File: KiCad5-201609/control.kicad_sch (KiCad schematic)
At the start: 23 parts, among them U304 DRV777DR

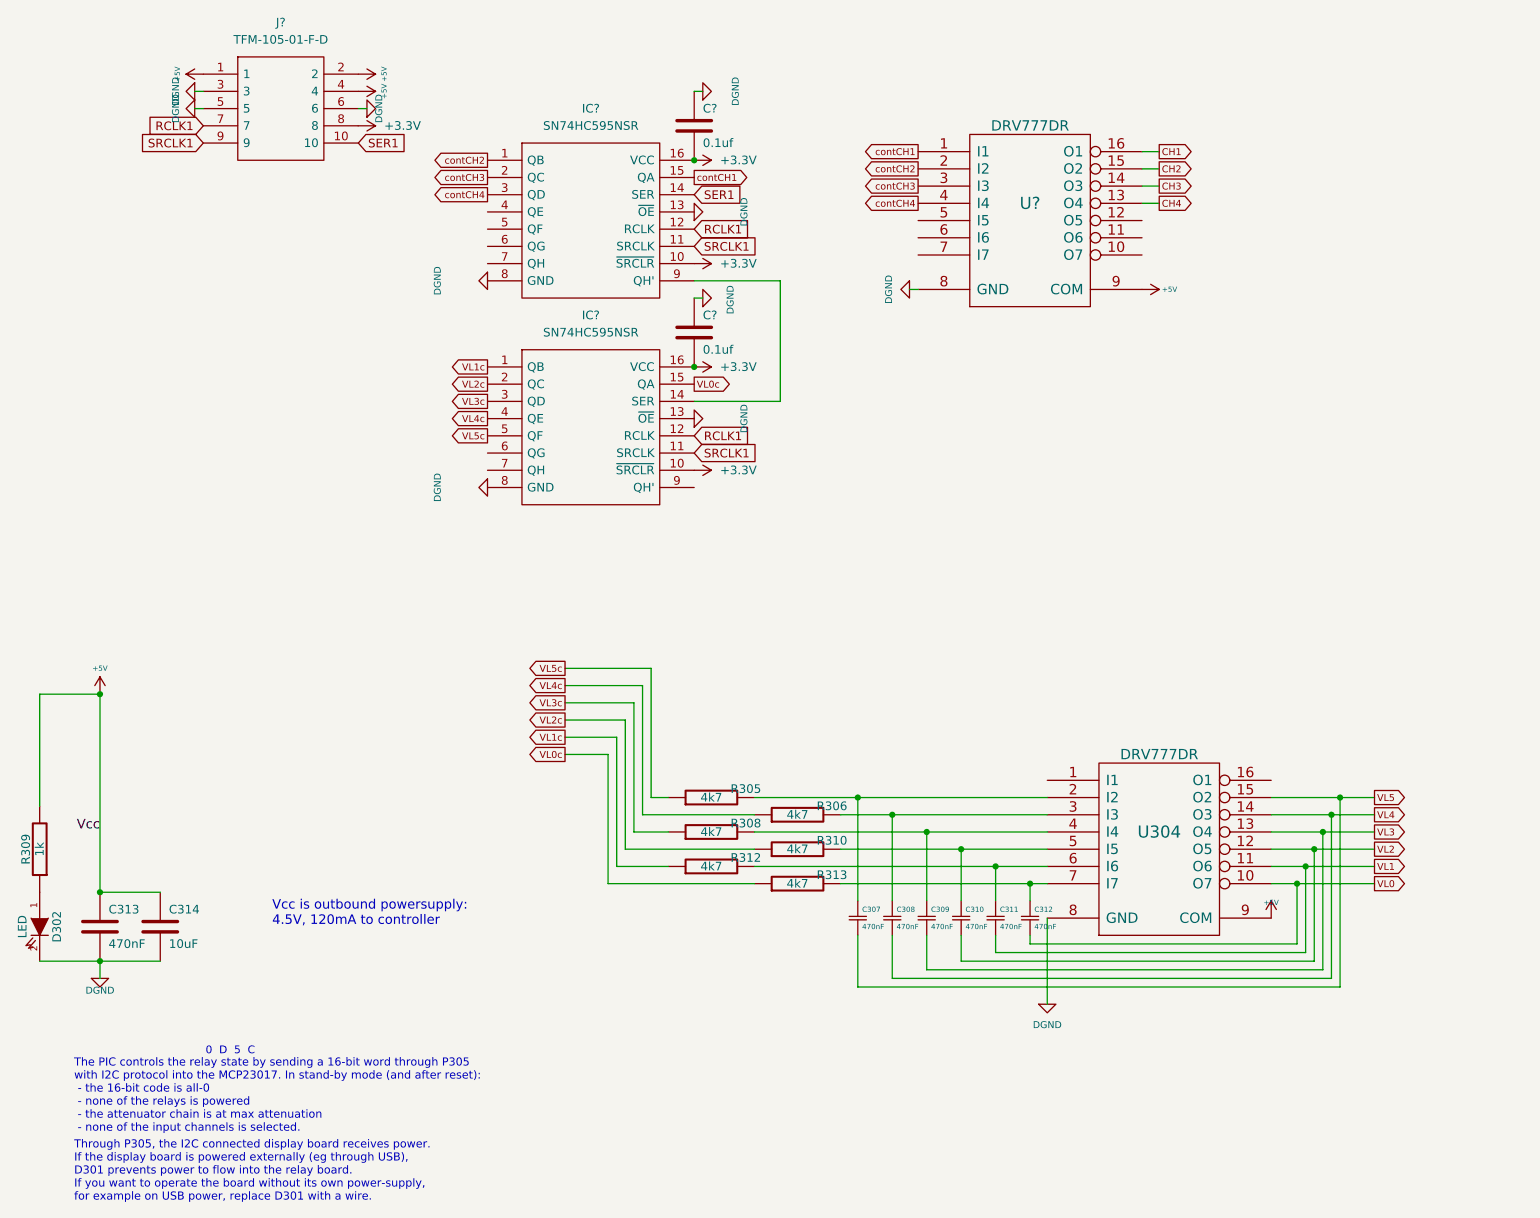
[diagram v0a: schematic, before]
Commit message: moved control to side, added electrolytic caps
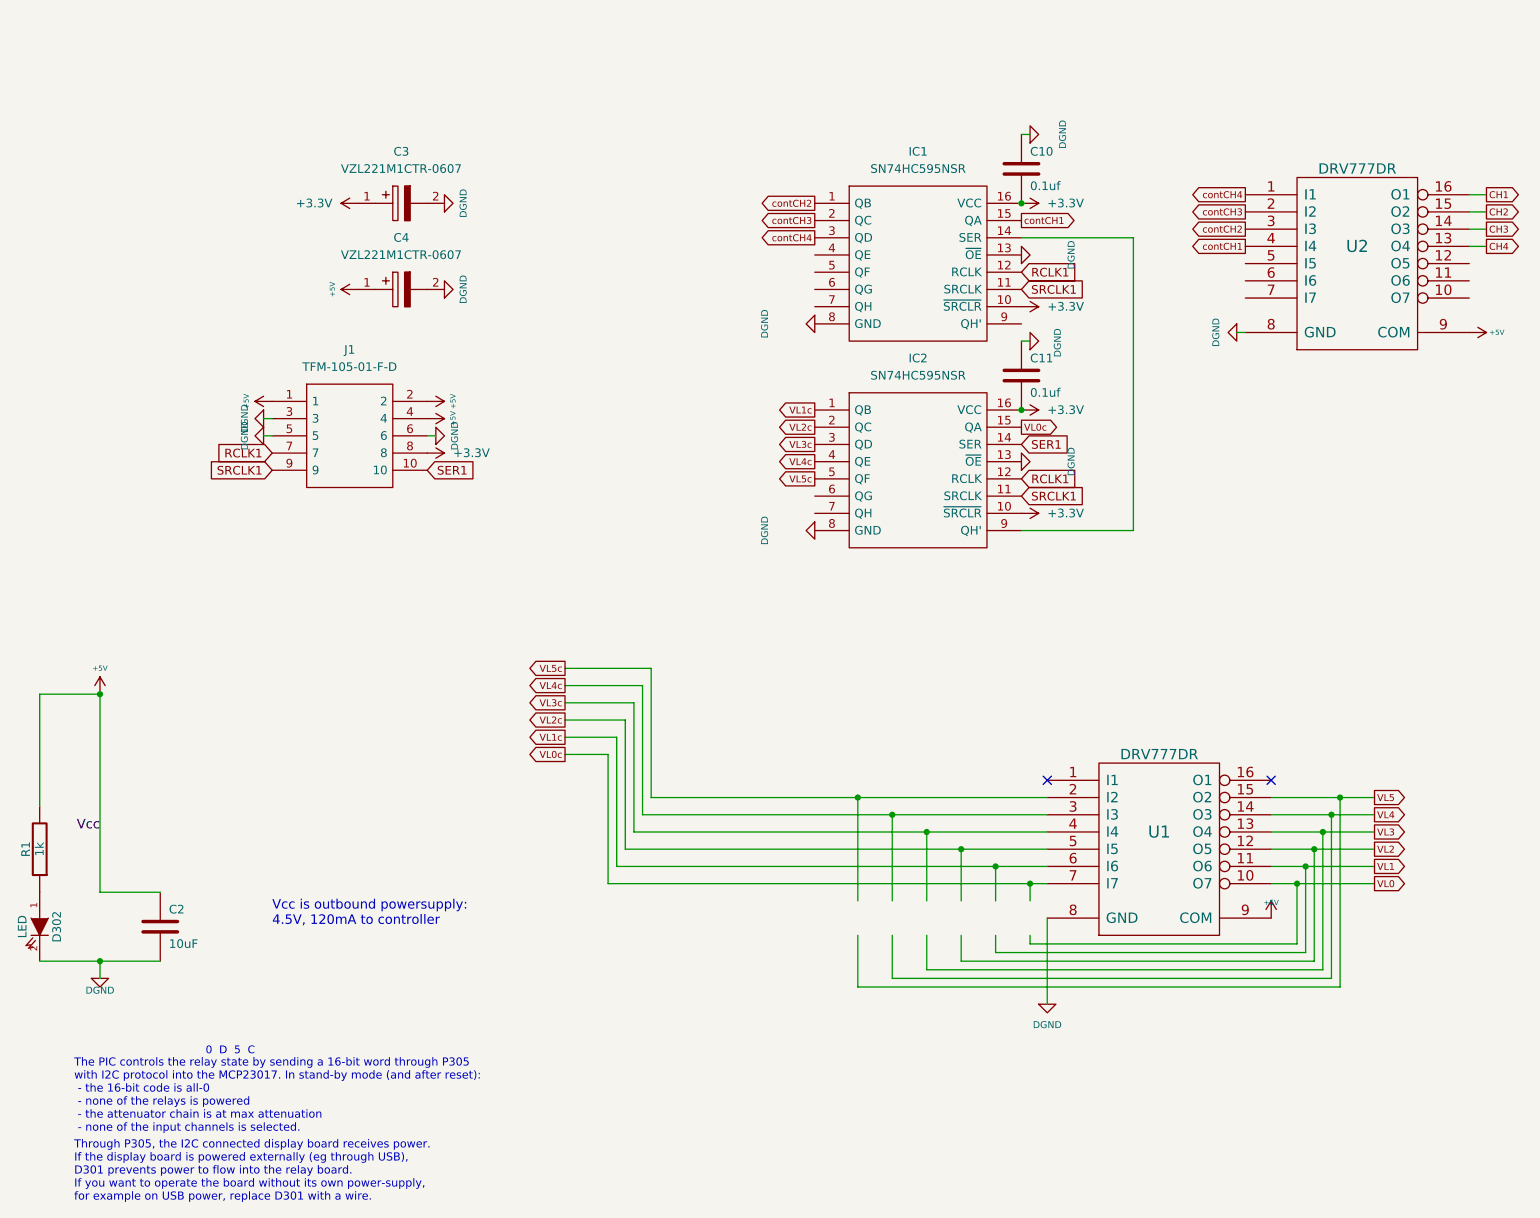
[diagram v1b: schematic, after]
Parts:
- removed C307, C308, C309, C310, C311, C312: 470nF, RlxPassiveFootprints:R0805, symbol relaixedPassive-rescue:Csmall
- removed C313: 470nF, RlxPassiveFootprints:R0805, symbol relaixedPassive-rescue:C
- removed R305, R306, R308, R310, R312, R313: 4k7, RlxPassiveFootprints:R0805, symbol relaixedPassive-rescue:R
- added C3, C4: VZL221M1CTR-0607, Samacsys:CAPAE660X800N, symbol Samacsys:VZL221M1CTR-0607
- gave numbers to parts that had none: 6
- renumbered C314 to C2, R309 to R1, U304 to U1
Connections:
- net +3.3V: now also C3.1
- net +5V: now also C4.1
- net DGND: now also C3.2, C4.2
- net SER1: now also IC2.14 (SER); no longer IC1.14 (SER)
- net VL0c: now also U1.7 (I7)
- net VL1c: now also U1.6 (I6)
- net VL2c: now also U1.5 (I5)
- net VL3c: now also U1.4 (I4)
- net VL4c: now also U1.3 (I3)
- net VL5c: now also U1.2 (I2)
- net contCH1: now also U2.4 (I4); no longer U2.1 (I1)
- net contCH2: now also U2.3 (I3); no longer U2.2 (I2)
- net contCH3: now also U2.2 (I2); no longer U2.3 (I3)
- net contCH4: now also U2.1 (I1); no longer U2.4 (I4)
- net at IC1.9 (QH'): no longer IC2.14 (SER)
- net at IC2.9 (QH'): now also IC1.14 (SER)
- no-connect marks 0 -> 2
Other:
- moved on the sheet: C10, C11, IC1, IC2, J1, U2

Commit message: added output rca option
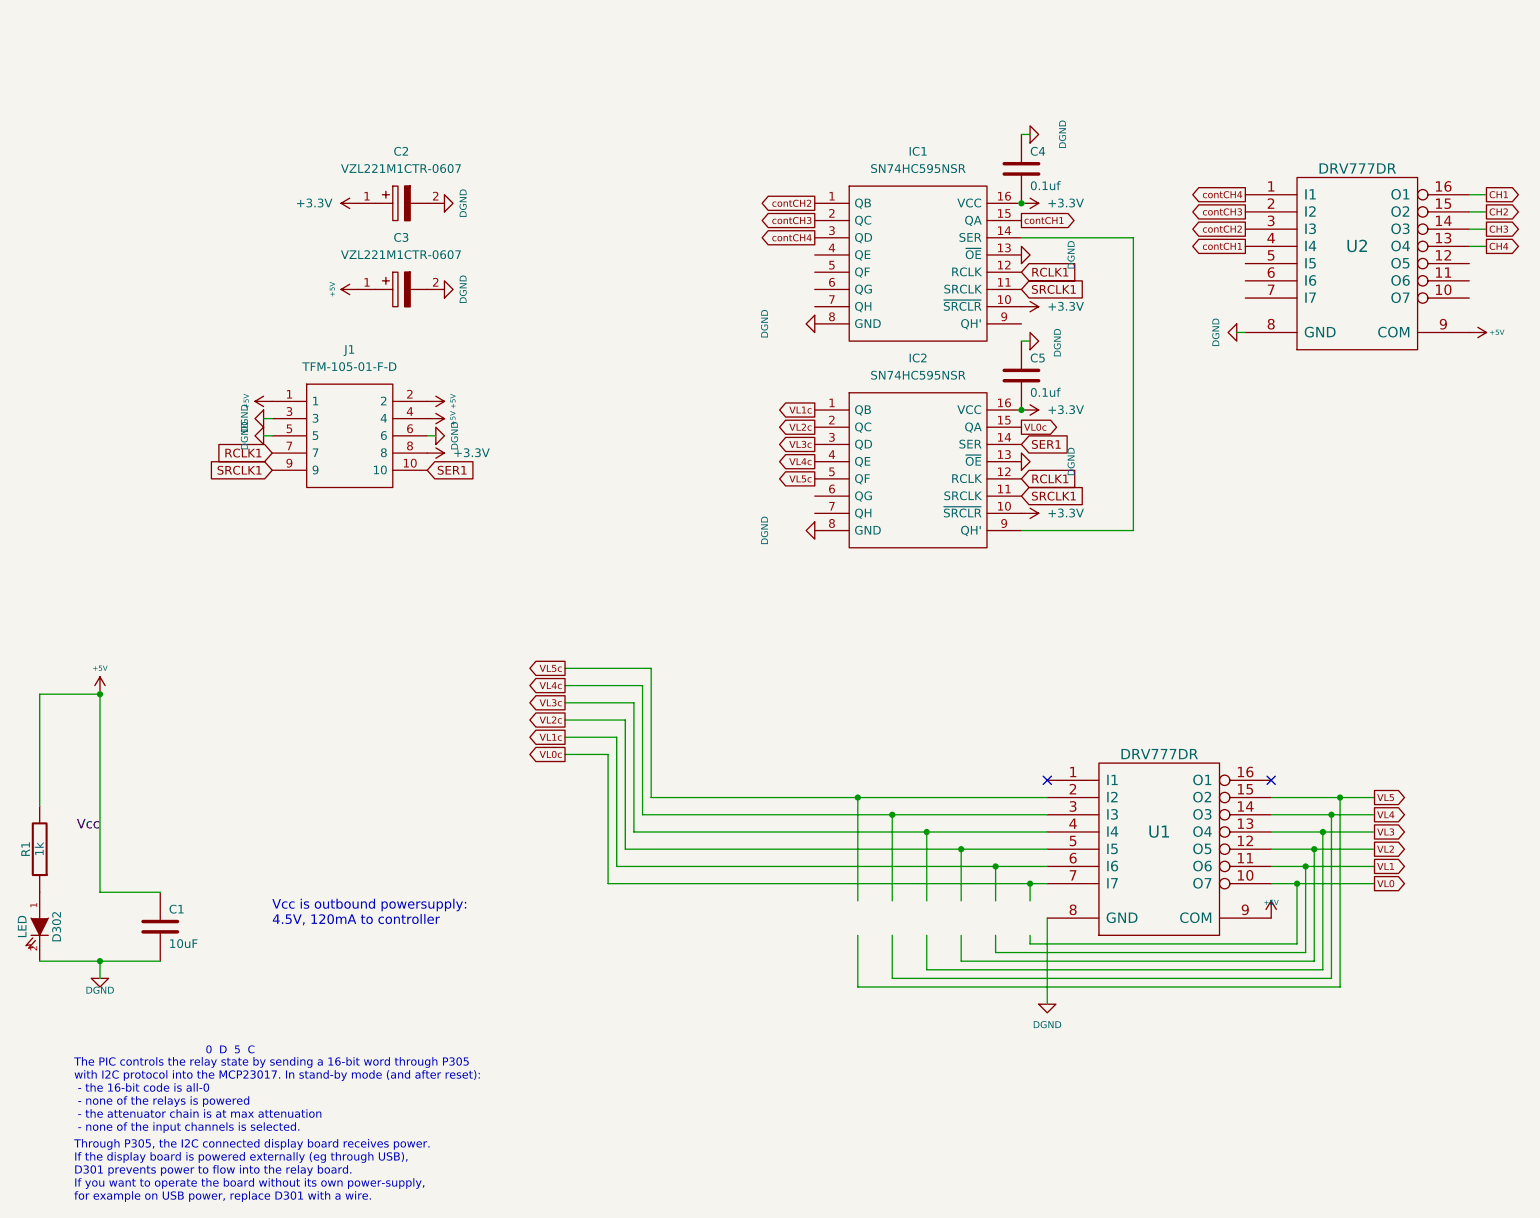
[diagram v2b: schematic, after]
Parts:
- renumbered C2 to C1, C3 to C2, C4 to C3, C10 to C4, C11 to C5
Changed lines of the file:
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@@
 		(on_board yes)
 		(dnp no)
-		(property "Reference" "C2"
+		(property "Reference" "C1"
 			(at 35.56 151.13 0)
 			(effects
@@
 			(project ""
 				(path "/97ae7532-5aa3-4e53-82e6-d486cce65bde/00000000-0000-0000-0000-00004f666988"
-					(reference "C2")
+					(reference "C1")
 					(unit 1)
 				)
@@
 		(dnp no)
 		(fields_autoplaced yes)
-		(property "Reference" "C4"
+		(property "Reference" "C3"
 			(at 69.85 52.07 0)
 			(effects
@@
 			(project "relaixedPassive"
 				(path "/97ae7532-5aa3-4e53-82e6-d486cce65bde/00000000-0000-0000-0000-00004f666988"
-					(reference "C4")
+					(reference "C3")
 					(unit 1)
 				)
@@
 		(on_board yes)
 		(dnp no)
-		(property "Reference" "C10"
+		(property "Reference" "C4"
 			(at 162.56 39.37 0)
 			(effects
@@
 			(project "relaixedPassive"
 				(path "/97ae7532-5aa3-4e53-82e6-d486cce65bde/00000000-0000-0000-0000-00004f666988"
-					(reference "C10")
+					(reference "C4")
 					(unit 1)
 				)
@@
 		(dnp no)
 		(fields_autoplaced yes)
-		(property "Reference" "C3"
+		(property "Reference" "C2"
 			(at 69.85 39.37 0)
 			(effects
@@
 			(project "relaixedPassive"
 				(path "/97ae7532-5aa3-4e53-82e6-d486cce65bde/00000000-0000-0000-0000-00004f666988"
-					(reference "C3")
+					(reference "C2")
 					(unit 1)
 				)
@@
 		(on_board yes)
 		(dnp no)
-		(property "Reference" "C11"
+		(property "Reference" "C5"
 			(at 162.56 69.85 0)
 			(effects
@@
 			(project "relaixedPassive"
 				(path "/97ae7532-5aa3-4e53-82e6-d486cce65bde/00000000-0000-0000-0000-00004f666988"
-					(reference "C11")
-					(unit 1)
-				)
+					(reference "C5")
+					(unit 1)
+				)
